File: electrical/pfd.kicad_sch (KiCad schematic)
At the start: 8 parts

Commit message: Interim check-in
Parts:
- added ELT: DTM3P, symbol Connector:Conn_01x03_Socket
- added ELT: DTM3R, symbol Connector:Conn_01x03_Pin
- added GTP: DTM4R, symbol Connector:Conn_01x04_Pin
- added GTP: DTM4P, symbol Connector:Conn_01x04_Socket
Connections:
- net ADSB_SERIAL_IN is gone; now on net ADSB_SERIAL_GND: GDU450.P4X02_47 (RS-232_IN_1)
- net ADSB_SERIAL_OUT is gone; now on net ADSB_SERIAL_GND: GDU450.P4X02_48 (RS-232_OUT_1)
- net AIRDATA_SERIAL_GND is gone; now on net ADSB_SERIAL_GND: GSU25.P252_11 (GROUND)
- net AIRDATA_SERIAL_OUT is gone; now on net ADSB_SERIAL_GND: GSU25.P252_15 (RS-232_TX_2)
- net AUDIO_HI is gone; now on net ADSB_SERIAL_GND: GDU450.P4X02_1 (MONO_AUDIO_OUT_HI)
- net AUDIO_LO is gone; now on net ADSB_SERIAL_GND: GDU450.P4X02_18 (MONO_AUDIO_OUT_LO)
- net CANBUS_HI_GMU_OUT is gone; now on net ADSB_SERIAL_GND: GMU11.P441_1 (CAN_BUS_HI)
- net CANBUS_HI_IN is gone; now on net ADSB_SERIAL_GND: G5.P51_1 (CAN-H), GDU450.P4X02_46 (CAN_BUS_HI), GSU25.P251_1 (CAN_H)
- net CANBUS_LO_GMU_OUT is gone; now on net ADSB_SERIAL_GND: GMU11.P441_2 (CAN_BUS_LO)
- net CANBUS_LO_IN is gone; now on net ADSB_SERIAL_GND: G5.P51_2 (CAN-L), GDU450.P4X02_45 (CAN_BUS_LO), GSU25.P251_2 (CAN_L)
- net EIS_SERIAL_GND is gone; now on net ADSB_SERIAL_GND: GDU450.P4X02_37 (SIGNAL_GROUND)
- net EIS_SERIAL_IN is gone; now on net ADSB_SERIAL_GND: GDU450.P4X02_23 (RS-232_IN_4)
- net EIS_SERIAL_OUT is gone; now on net ADSB_SERIAL_GND: GDU450.P4X02_40 (RS-232_OUT_4)
- net NAV_CONNEXT_SERIAL_GND is gone; now on net ADSB_SERIAL_GND: GDU450.P4X02_36 (SIGNAL_GROUND)
- net NAV_CONNEXT_SERIAL_IN is gone; now on net ADSB_SERIAL_GND: GDU450.P4X02_29 (RS-232_IN_3)
- net NAV_CONNEXT_SERIAL_OUT is gone; now on net ADSB_SERIAL_GND: GDU450.P4X02_13 (RS-232_OUT_3)
- net NAV_MAPMX_SERIAL_GND is gone; now on net ADSB_SERIAL_GND: G5.P51_6 (SIGNAL_GROUND), GDU450.P4X02_35 (SIGNAL_GROUND)
- net NAV_MAPMX_SERIAL_IN is gone; now on net ADSB_SERIAL_GND: G5.P51_4 (RS-232_RX_1), GDU450.P4X02_14 (RS-232_IN_2)
- net NAV_MAPMX_SERIAL_OUT is gone; now on net ADSB_SERIAL_GND: GDU450.P4X02_30 (RS-232_OUT_2)
- net ADSB_SERIAL_GND: now also GDU450.P4X01_4 (RS-232_RX), GDU450.P4X01_5 (RS-232_TX), GDU450.P4X01_6 (SIGNAL_GND), GDU450.P4X02_41 (RS-232_OUT_5), GDU450.P4X02_44 (SIGNAL_GROUND), GSU25.P251_4 (RS-232_RX_1), GSU25.P251_5 (RS-232_TX_1), GSU25.P251_6 (SIGNAL_GROUND), ELT.1 (Pin_1), ELT.2 (Pin_2)
- net ELT_SERIAL_GND: now also ELT.2 (Pin_2); no longer GDU450.P4X02_44 (SIGNAL_GROUND)
- net ELT_SERIAL_OUT: now also ELT.1 (Pin_1); no longer GDU450.P4X02_41 (RS-232_OUT_5)
- net W: now reaches GSU25.P252_1 (OAT_POWER)
- net W: now also GTP.1 (Pin_1); no longer GTP59. (LOW)
- net B: now reaches GSU25.P252_2 (OAT_HIGH)
- net B: now also GTP.2 (Pin_2); no longer GTP59. (LOW)
- net O: now reaches GSU25.P252_3 (OAT_LOW)
- net O: now also GTP.3 (Pin_3); no longer GTP59. (LOW)
- new net: GTP.2 (Pin_2), GTP59.B (SENSE)
- new net: GTP.3 (Pin_3), GTP59.O (LOW)
- new net: GTP.1 (Pin_1), GTP59.W (POWER)
- new net Earth: GTP.4 (Pin_4)
- new net GNDS: ELT.3 (Pin_3)
- no-connect marks 21 -> 22
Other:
- note added: "Only a 2 conductor wire"

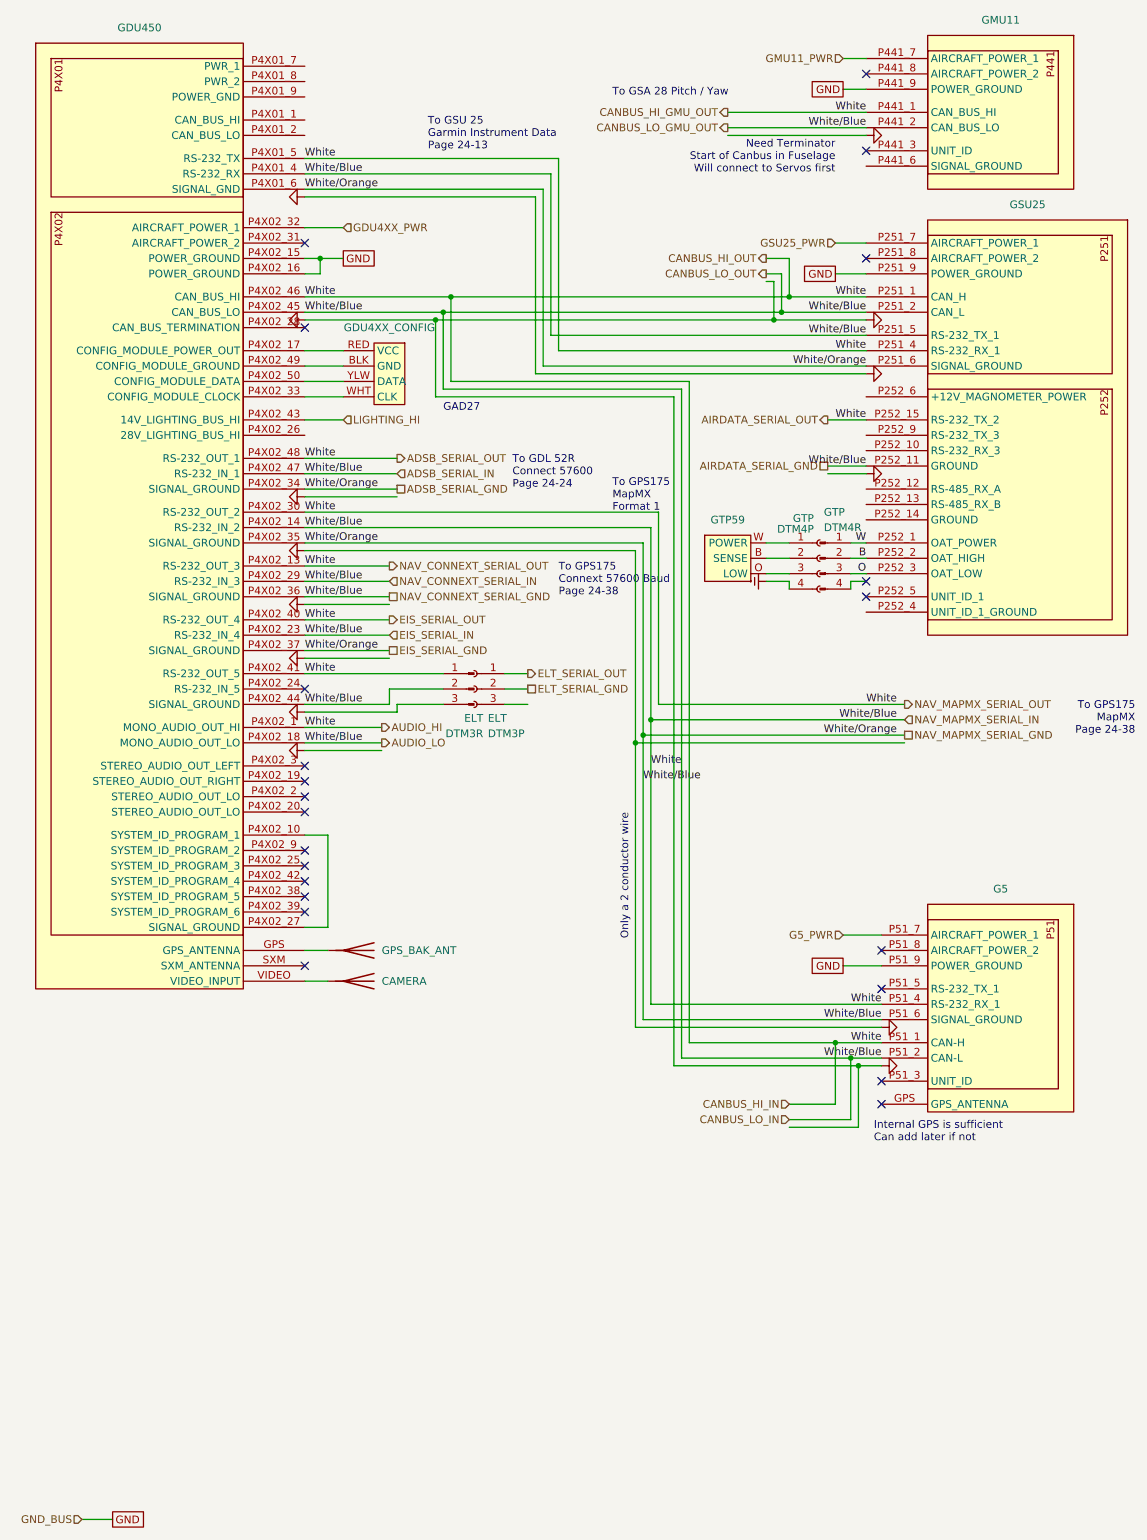
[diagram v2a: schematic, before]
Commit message: Went through and changed a lot from discussions and tradeoffs. Added GTX 330, rmemoved Connext from GDU and added to GPS 175 from GDL 52. Added relay for smoke and to not use GAD 27. Added Tach sensor for SureFly. Added carb heat. Added connectors to run panel disconnected.
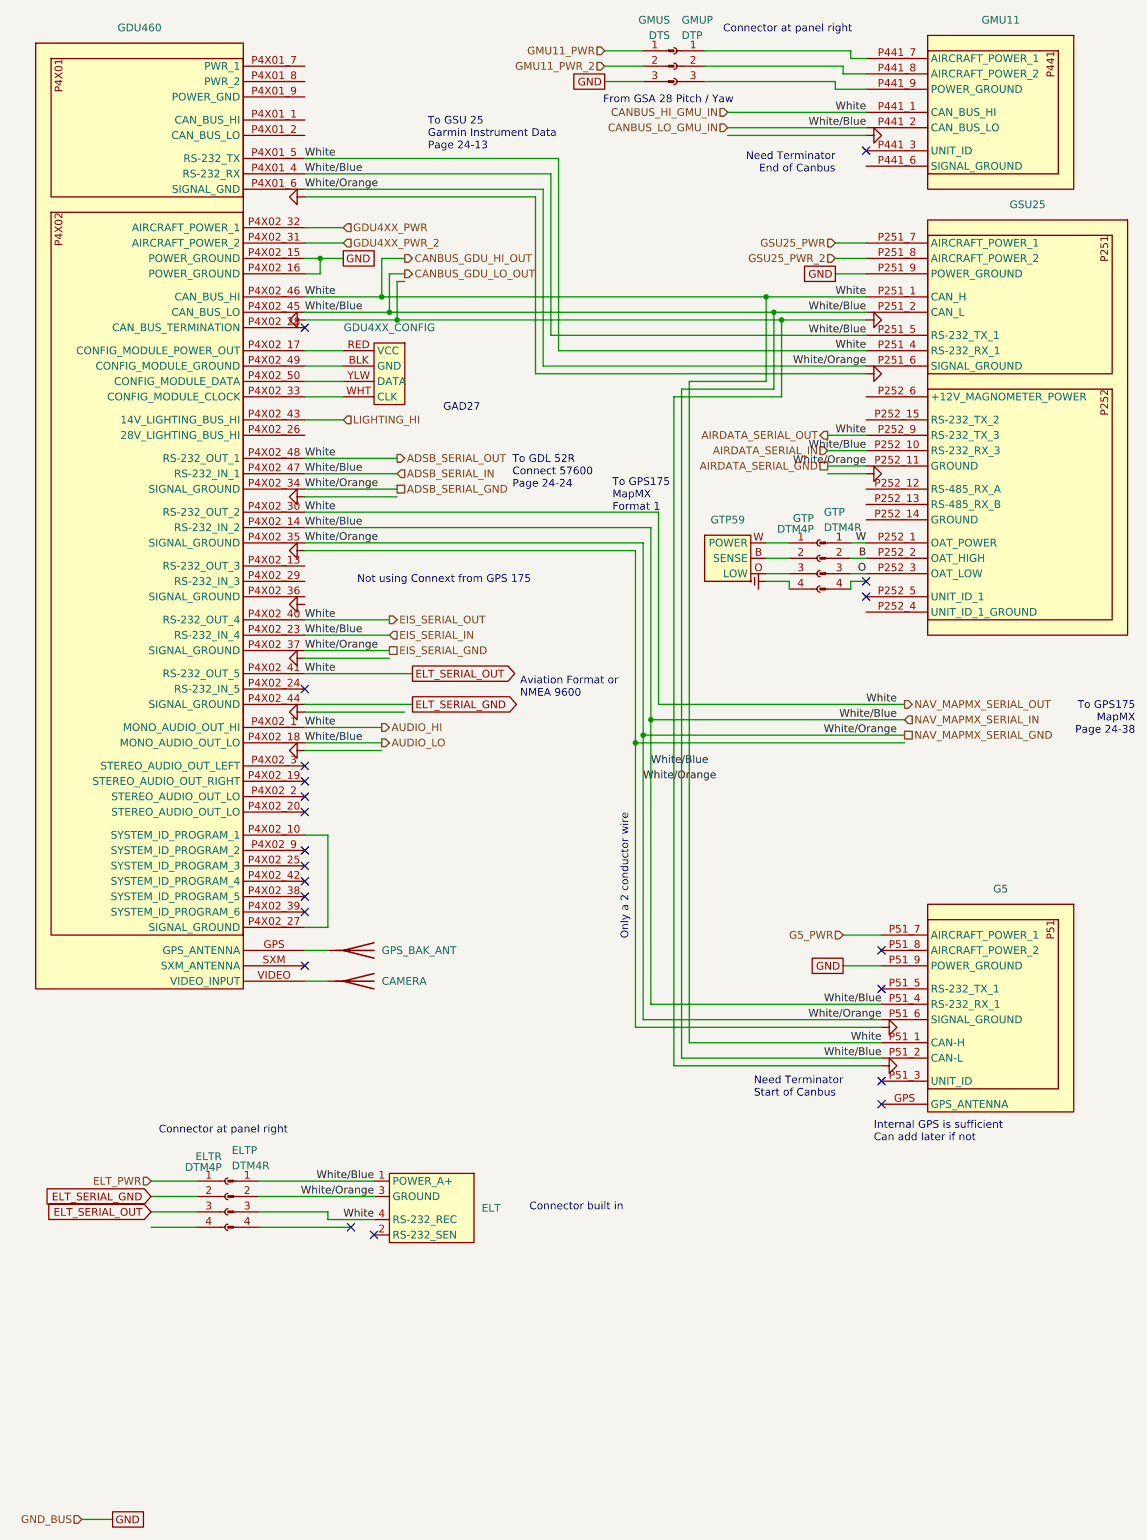
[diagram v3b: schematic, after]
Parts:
- removed ELT: DTM3P, symbol Connector:Conn_01x03_Socket
- removed ELT: DTM3R, symbol Connector:Conn_01x03_Pin
- added ELT: ~, symbol flyerx:ACK_E-04
- added ELTP: DTM4R, symbol Connector:Conn_01x04_Pin
- added ELTR: DTM4P, symbol Connector:Conn_01x04_Socket
- added GMUP: DTP, symbol Connector:Conn_01x03_Socket
- added GMUS: DTS, symbol Connector:Conn_01x03_Pin
- renumbered GDU450 to GDU460
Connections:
- net ADSB_SERIAL_GND: now also ELT.3 (GROUND), ELTP.2 (Pin_2); no longer G5.P51_1 (CAN-H), G5.P51_2 (CAN-L), G5.P51_4 (RS-232_RX_1), GDU460.P4X01_4 (RS-232_RX), GDU460.P4X01_5 (RS-232_TX), GDU460.P4X02_1 (MONO_AUDIO_OUT_HI), GDU460.P4X02_13 (RS-232_OUT_3), GDU460.P4X02_14 (RS-232_IN_2), GDU460.P4X02_18 (MONO_AUDIO_OUT_LO), GDU460.P4X02_23 (RS-232_IN_4), GDU460.P4X02_29 (RS-232_IN_3), GDU460.P4X02_30 (RS-232_OUT_2), GDU460.P4X02_36 (SIGNAL_GROUND), GDU460.P4X02_40 (RS-232_OUT_4), GDU460.P4X02_41 (RS-232_OUT_5), GDU460.P4X02_44 (SIGNAL_GROUND), GDU460.P4X02_45 (CAN_BUS_LO), GDU460.P4X02_46 (CAN_BUS_HI), GDU460.P4X02_47 (RS-232_IN_1), GDU460.P4X02_48 (RS-232_OUT_1), GMU11.P441_1 (CAN_BUS_HI), GMU11.P441_2 (CAN_BUS_LO), GSU25.P251_1 (CAN_H), GSU25.P251_2 (CAN_L), GSU25.P251_4 (RS-232_RX_1), GSU25.P251_5 (RS-232_TX_1), GSU25.P252_15 (RS-232_TX_2)
- net ELT_SERIAL_GND: now also GDU460.P4X02_44 (SIGNAL_GROUND), ELTR.2 (Pin_2)
- net ELT_SERIAL_OUT: now also G5.P51_1 (CAN-H), GDU460.P4X01_5 (RS-232_TX), GDU460.P4X02_1 (MONO_AUDIO_OUT_HI), GDU460.P4X02_30 (RS-232_OUT_2), GDU460.P4X02_40 (RS-232_OUT_4), GDU460.P4X02_41 (RS-232_OUT_5), GDU460.P4X02_46 (CAN_BUS_HI), GDU460.P4X02_48 (RS-232_OUT_1), GMU11.P441_1 (CAN_BUS_HI), GSU25.P251_1 (CAN_H), GSU25.P251_4 (RS-232_RX_1), GSU25.P252_9 (RS-232_TX_3), ELT.4 (RS-232_REC), ELTP.3 (Pin_3), ELTR.3 (Pin_3)
- net GMU11_PWR: now also GMUS.1 (Pin_1); no longer GMU11.P441_7 (AIRCRAFT_POWER_1)
- net GND: now also GMUS.3 (Pin_3); no longer GMU11.P441_9 (POWER_GROUND)
- net GSU25_PWR_2: now reaches GSU25.P251_8 (AIRCRAFT_POWER_2)
- net ADSB_SERIAL_IN: now reaches GSU25.P252_10 (RS-232_RX_3)
- net ADSB_SERIAL_IN: now also G5.P51_2 (CAN-L), G5.P51_4 (RS-232_RX_1), GDU460.P4X01_4 (RS-232_RX), GDU460.P4X02_14 (RS-232_IN_2), GDU460.P4X02_18 (MONO_AUDIO_OUT_LO), GDU460.P4X02_23 (RS-232_IN_4), GDU460.P4X02_45 (CAN_BUS_LO), GDU460.P4X02_47 (RS-232_IN_1), GMU11.P441_2 (CAN_BUS_LO), GSU25.P251_2 (CAN_L), GSU25.P251_5 (RS-232_TX_1), ELT.1 (POWER_A+), ELTP.1 (Pin_1)
- net GDU4XX_PWR_2: now reaches GDU460.P4X02_31 (AIRCRAFT_POWER_2)
- net at GMU11.P441_8 (AIRCRAFT_POWER_2): now also GMUP.2 (Pin_2)
- new net: GMU11.P441_7 (AIRCRAFT_POWER_1), GMUP.1 (Pin_1)
- new net: GMU11.P441_9 (POWER_GROUND), GMUP.3 (Pin_3)
- new net ELT_PWR: ELTR.1 (Pin_1)
- new net GMU11_PWR_2: GMUS.2 (Pin_2)
- no-connect marks 22 -> 21
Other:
- note added: "Aviation Format or NMEA 9600"
- note added: "Connector at panel right"
- note added: "Connector built in"
- note added: "From GSA 28 Pitch / Yaw"
- note added: "Need Terminator End of Canbus"
- note added: "Need Terminator Start of Canbus"
- note added: "Not using Connext from GPS 175"
- note removed: "Need Terminator Start of Canbus in Fuselage Will connect to Servos first"
- note removed: "To GPS175 Connext 57600 Baud Page 24-38"
- note removed: "To GSA 28 Pitch / Yaw"

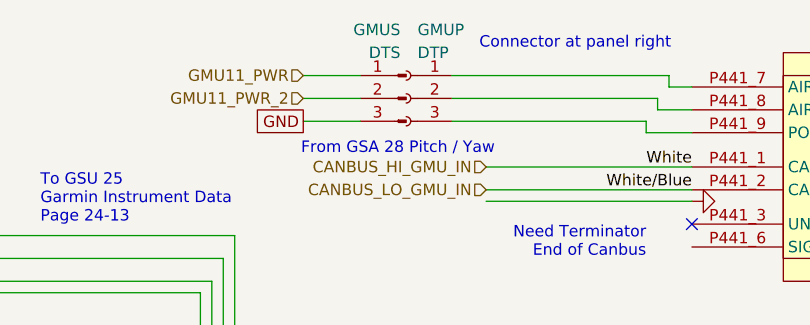
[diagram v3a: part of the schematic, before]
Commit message: Assumed engine connector is sufficient for wiring on bench..
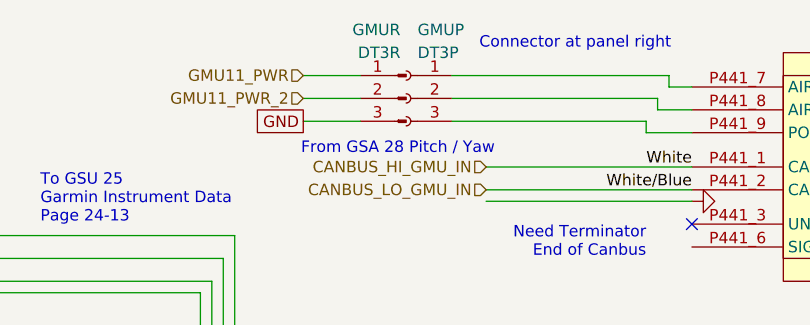
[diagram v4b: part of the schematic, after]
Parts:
- GMUP: value DTP -> DT3P
- GMUR: renamed from GMUS; value DTS -> DT3R
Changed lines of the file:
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@@
 	(title_block
 		(title "PFD & ADAHRS")
-		(date "2025-12-24")
-		(rev "1.2")
+		(date "2026-01-03")
+		(rev "1.2.3")
 		(company "N877RV")
 	)
@@
 		(on_board yes)
 		(dnp no)
-		(property "Reference" "GMUS"
+		(property "Reference" "GMUR"
 			(at 122.555 13.97 0)
 			(effects
@@
 			)
 		)
-		(property "Value" "DTS"
+		(property "Value" "DT3R"
 			(at 122.555 16.51 0)
 			(effects
@@
 			(project "electrical"
 				(path "/e8ec215a-dbe2-4eba-a577-e50a0a128049/633b5331-dc3f-449e-8212-24f89753723c"
-					(reference "GMUS")
+					(reference "GMUR")
 					(unit 1)
 				)
@@
 			)
 		)
-		(property "Value" "DTP"
+		(property "Value" "DT3P"
 			(at 124.46 16.51 0)
 			(effects

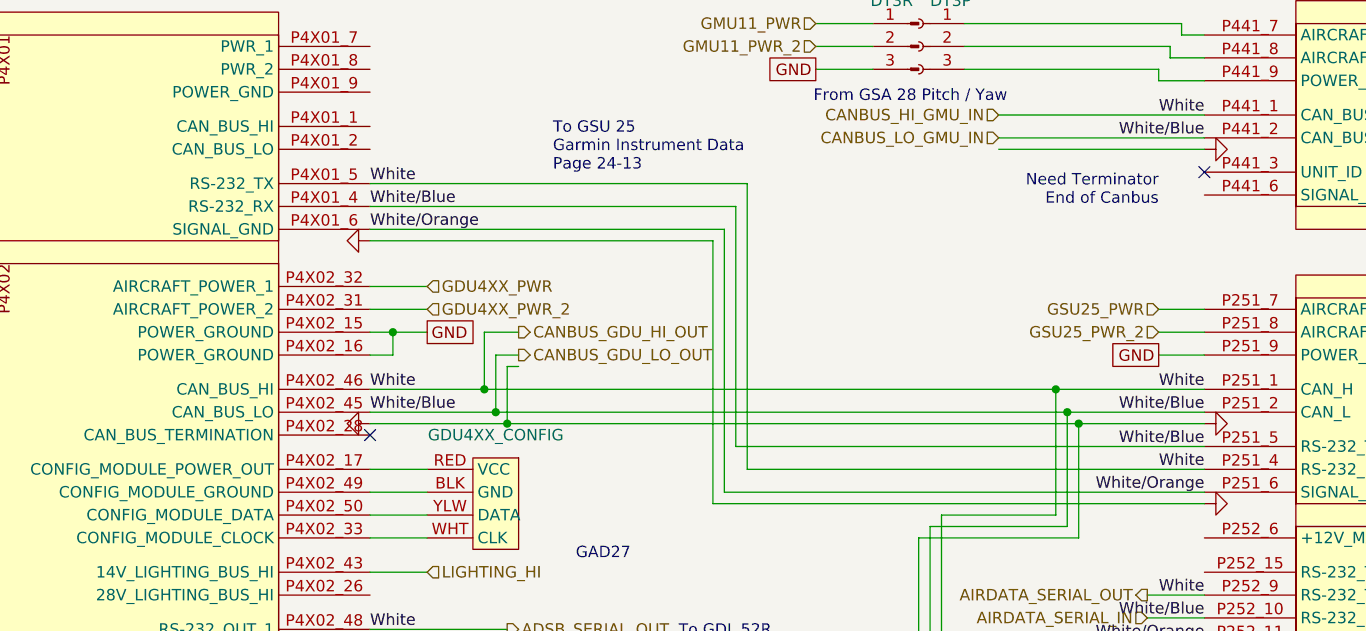
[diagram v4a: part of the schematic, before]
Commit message: Changed comms PTT and removed shield to TRS plugs. Fixed backwards GDU TX/RX wiring for GSU.
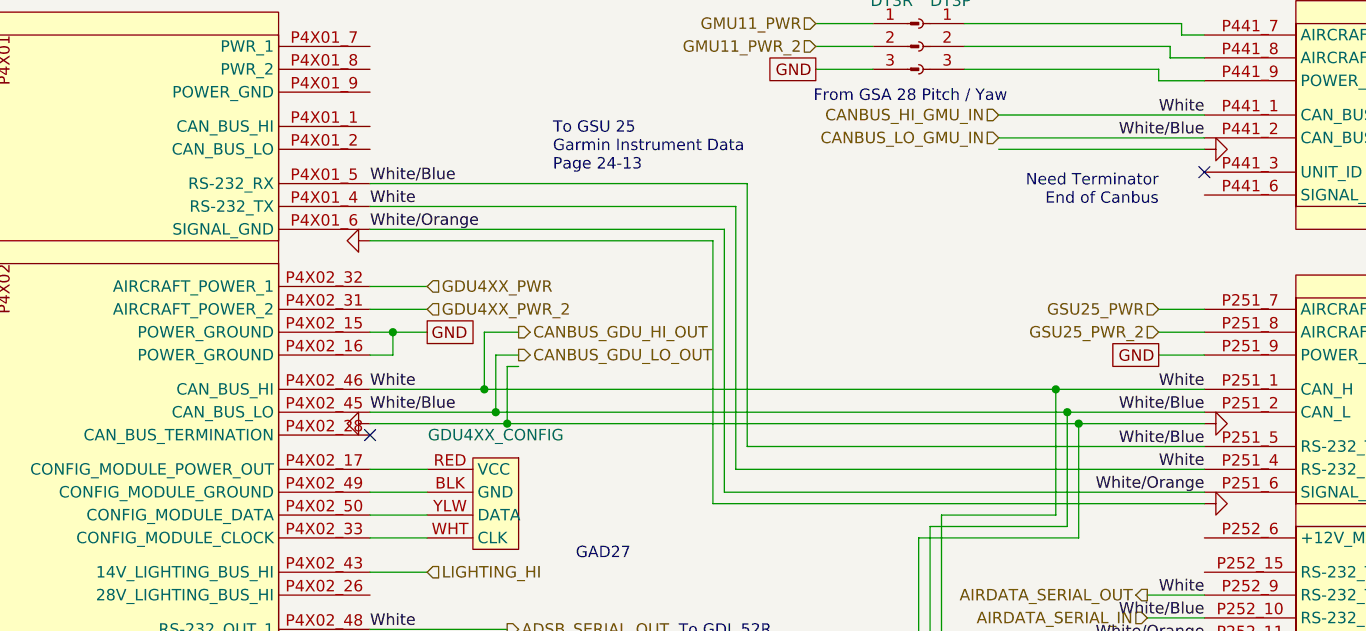
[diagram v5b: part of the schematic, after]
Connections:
- net ADSB_SERIAL_IN: now also GDU460.P4X01_5 (RS-232_RX); no longer GDU460.P4X01_4 (RS-232_RX)
- net ELT_SERIAL_OUT: now also GDU460.P4X01_4 (RS-232_TX); no longer GDU460.P4X01_5 (RS-232_TX)
